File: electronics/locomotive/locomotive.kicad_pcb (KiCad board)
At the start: 2 copper layers, 16 x 64 mm, 0 parts

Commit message: electronics: locomotive: Board Rev 1.0
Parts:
- added 10: 100n, Capacitors_SMD:C_0603, F.Cu at (152.0, 92.0)
- added 10: 10k, Resistors_SMD:R_0603, F.Cu at (147.5, 112.5)
- added 11: 100n, Capacitors_SMD:C_0603, F.Cu at (144.0, 92.5)
- added 11: 10k, Resistors_SMD:R_0603, F.Cu at (156.2, 104.5)
- added 12: 10k, Resistors_SMD:R_0603, F.Cu at (144.0, 130.8)
- added 12: 1u, Capacitors_SMD:C_0603, F.Cu at (145.8, 93.5)
- added 13: 2u2, Capacitors_SMD:C_0603, F.Cu at (154.2, 125.5)
- added 13: 33k2, Resistors_SMD:R_0603, F.Cu at (151.2, 125.5)
- added 14: 26k1, Resistors_SMD:R_0603, F.Cu at (152.8, 125.5)
- added 15: 1k, Resistors_SMD:R_0603, F.Cu at (156.2, 76.2)
- added 16: 1k, Resistors_SMD:R_0603, F.Cu at (154.8, 76.2)
- added 19: 1k5, Resistors_SMD:R_0603, F.Cu at (155.5, 66.0)
- added 20: 10k, Resistors_SMD:R_0603, F.Cu at (144.5, 66.0)
- added C1: 2u2, Capacitors_SMD:C_0603, F.Cu at (147.5, 108.5)
- added C2: 2u2, Capacitors_SMD:C_0603, F.Cu at (155.5, 109.0)
- added C3: 100n, Capacitors_SMD:C_0603, F.Cu at (152.0, 90.5)
- added C4: 10p, Capacitors_SMD:C_0603, F.Cu at (148.2, 88.2)
- added C5: 10p, Capacitors_SMD:C_0603, F.Cu at (145.0, 91.5)
- added C6: 4u7, Capacitors_SMD:C_0603, F.Cu at (147.5, 111.0)
- added C7: 100n, Capacitors_SMD:C_0603, F.Cu at (143.8, 104.5)
- added C8: 100n, Capacitors_SMD:C_0603, F.Cu at (147.5, 109.8)
- added C9: 100n, Capacitors_SMD:C_0603, F.Cu at (156.2, 107.0)
- added D1: CDBHM240L-HF, bcan:TO-269AA, F.Cu at (150.0, 78.0)
- added D2: CUS08F30, Diodes_SMD:D_SOD-323, F.Cu at (145.5, 125.0)
- added D3: 1N4148, Diodes_SMD:D_SOD-523, F.Cu at (154.0, 66.0)
- added J1: PIN[1..32], bcan:Castellations_1x32_Pitch2.00mm, F.Cu at (142.0, 69.0)
- added J2: PIN[33..64], bcan:Castellations_1x32_Pitch2.00mm, F.Cu at (158.0, 131.0)
- added J3: JTAG, Pin_Headers:Pin_Header_Straight_2x05_Pitch1.27mm_SMD, B.Cu at (150.0, 90.0)
- added J4: USB_OTG, bcan:USB_Micro-B_Amphenol_10118192, F.Cu at (150.0, 130.6)
- added J5: RAILS, bcan:Castellations_1x02_Pitch2.00mm, F.Cu at (142.0, 65.0)
- added J6: MOTOR, bcan:Castellations_1x02_Pitch2.00mm, F.Cu at (158.0, 67.0)
- added J7: TRAIN, Pin_Headers:Pin_Header_Straight_2x04_Pitch2.54mm_SMD, B.Cu at (150.0, 71.5)
- added J8: IR, Connectors_JST:JST_GH_BM04B-GHS-TBT_04x1.25mm_Straight, F.Cu at (150.0, 120.0)
- added J9: TOF, Connectors_JST:JST_GH_SM04B-GHS-TB_04x1.25mm_Angled, F.Cu at (150.0, 84.0)
- added JP1: BOOT0, bcan:Solder_Jumper_NC, B.Cu at (150.0, 77.8)
- added JP2: BOOT1, bcan:Solder_Jumper_NC, B.Cu at (149.0, 123.8)
- added JP3: VCAP1, bcan:Solder_Jumper_NO, B.Cu at (149.2, 108.0)
- added JP4: VCAP2, bcan:Solder_Jumper_NO, B.Cu at (150.8, 108.0)
- added JP5: USB_VBUS, bcan:Solder_Jumper_NC, B.Cu at (151.0, 123.8)
- added L1: 600, Capacitors_SMD:C_0603, F.Cu at (143.8, 95.5)
- added Q1: MMBT2222A, TO_SOT_Packages_SMD:SOT-23, F.Cu at (155.2, 73.2)
- added Q2: MMBT2222A, TO_SOT_Packages_SMD:SOT-23, F.Cu at (144.8, 69.8)
- added Q3: DMG6601LVT, TO_SOT_Packages_SMD:SOT-23-6, F.Cu at (155.2, 69.8)
- added Q4: DMG6601LVT, TO_SOT_Packages_SMD:SOT-23-6, F.Cu at (144.8, 73.2)
- added R1: 10k, Resistors_SMD:R_0603, F.Cu at (154.8, 78.8)
- added R17: 100, Resistors_SMD:R_2512, F.Cu at (151.8, 71.5)
- added R18: 100, Resistors_SMD:R_2512, F.Cu at (148.2, 71.5)
- added R2: 10k, Resistors_SMD:R_0603, F.Cu at (149.5, 115.0)
- added R3: 10k, Resistors_SMD:R_0603, F.Cu at (152.0, 89.0)
- added R4: 13k3, Resistors_SMD:R_0603, F.Cu at (144.2, 86.2)
- added R5: 2k8, Resistors_SMD:R_0603, F.Cu at (144.2, 87.8)
- added R8: 4k7, Resistors_SMD:R_0603, F.Cu at (147.5, 115.5)
- added R9: 4k7, Resistors_SMD:R_0603, F.Cu at (147.5, 114.0)
- added U1: STM32F405RGTx, Housings_QFP:TQFP-64_10x10mm_Pitch0.5mm, F.Cu at (150.0, 100.0)
- added U2: M95512-RDW6TP, Housings_SSOP:TSSOP-8_4.4x3mm_Pitch0.65mm, F.Cu at (153.0, 112.0)
- added U5: SPX3819M5, TO_SOT_Packages_SMD:SOT-23-5, F.Cu at (148.5, 125.0)
- added U7: TLP293, Housings_SSOP:SOP-4_4.4x2.8mm_Pitch1.27mm, F.Cu at (149.2, 66.0)
- added Y1: 16MHz, Crystals:Crystal_SMD_3225-4pin_3.2x2.5mm, F.Cu at (147.0, 90.2)
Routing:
- net GND: track 0.00 -> 222.6 mm, vias 0 -> 16
- net 2V8: track 0.00 -> 124.7 mm, vias 0 -> 4
- net VCC: track 0.00 -> 93.9 mm, vias 0 -> 2
- net PA10: track 0.00 -> 51.8 mm, vias 0 -> 2
- net PA11: track 0.00 -> 48.7 mm, vias 0 -> 2
- net PA12: track 0.00 -> 47.3 mm, vias 0 -> 2
- net PB11: track 0.00 -> 47.1 mm, vias 0 -> 2
- net PB12: track 0.00 -> 46.7 mm, vias 0 -> 1
- net PB10: track 0.00 -> 45.0 mm, vias 0 -> 2
- net PB14: track 0.00 -> 43.8 mm, vias 0 -> 2
- net NRST: track 0.00 -> 42.8 mm, vias 0 -> 2
- net PC13: track 0.00 -> 39.1 mm, vias 0 -> 1
- net PA13: track 0.00 -> 37.5 mm, vias 0 -> 1
- net PB13: track 0.00 -> 35.1 mm
- net BOOT0: track 0.00 -> 33.8 mm
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- added copper zone on F.Cu, net 2V8
- added copper zone on B.Cu, net GND
- added copper zone on F.Cu, net GND
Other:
- board size 16 x 64 mm -> 16 x 68 mm
- net class Default: clearance 0.2 -> 0.16; trace_width 0.25 -> 0.2
- net class Motor added: clearance 0.16, trace_width 0.6, via_dia 0.6, via_drill 0.4
- net class Power added: clearance 0.16, trace_width 0.3, via_dia 0.6, via_drill 0.4
- rule trace_clearance: 0.2 -> 0.16
- board text added: "+"
- board text added: "-"
- board text added: "2V8"
- board text added: "5V"
- board text added: "B8"
- board text added: "B9"
- board text added: "BOOT0"
- board text added: "BOOT1"
- board text added: "C13"
- board text added: "C14"
- board text added: "C15"
- board text added: "F-"
- board text added: "GND"
- board text added: "IR"
- board text added: "JST-GH"
- board text added: "JTAG"
- board text added: "L"
- board text added: "Locomotive Rev 1.0"
- board text added: "MOTOR"
- board text added: "NRST"
- board text added: "PA0"
- board text added: "PA1"
- board text added: "PA10"
- board text added: "PA11"
- board text added: "PA12"
- board text added: "PA13"
- board text added: "PA14"
- board text added: "PA15"
- board text added: "PA2"
- board text added: "PA3"
- board text added: "PA4"
- board text added: "PA5"
- board text added: "PA6"
- board text added: "PA7"
- board text added: "PA8"
- board text added: "PA9"
- board text added: "PB0"
- board text added: "PB1"
- board text added: "PB10"
- board text added: "PB11"
- board text added: "PB12"
- board text added: "PB13"
- board text added: "PB14"
- board text added: "PB15"
- board text added: "PB2"
- board text added: "PB3"
- board text added: "PB4"
- board text added: "PB5"
- board text added: "PB6"
- board text added: "PB7"
- board text added: "PC0"
- board text added: "PC1"
- board text added: "PC10"
- board text added: "PC11"
- board text added: "PC12"
- board text added: "PC2"
- board text added: "PC3"
- board text added: "PC4"
- board text added: "PC5"
- board text added: "PC6"
- board text added: "PC7"
- board text added: "PC8"
- board text added: "PC9"
- board text added: "PD2"
- board text added: "R"
- board text added: "R-"
- board text added: "RAILS"
- board text added: "TOF"
- board text added: "VBAT"
- board text added: "VCAP"
- board text added: "VCC"
- board text added: "bcan.io"

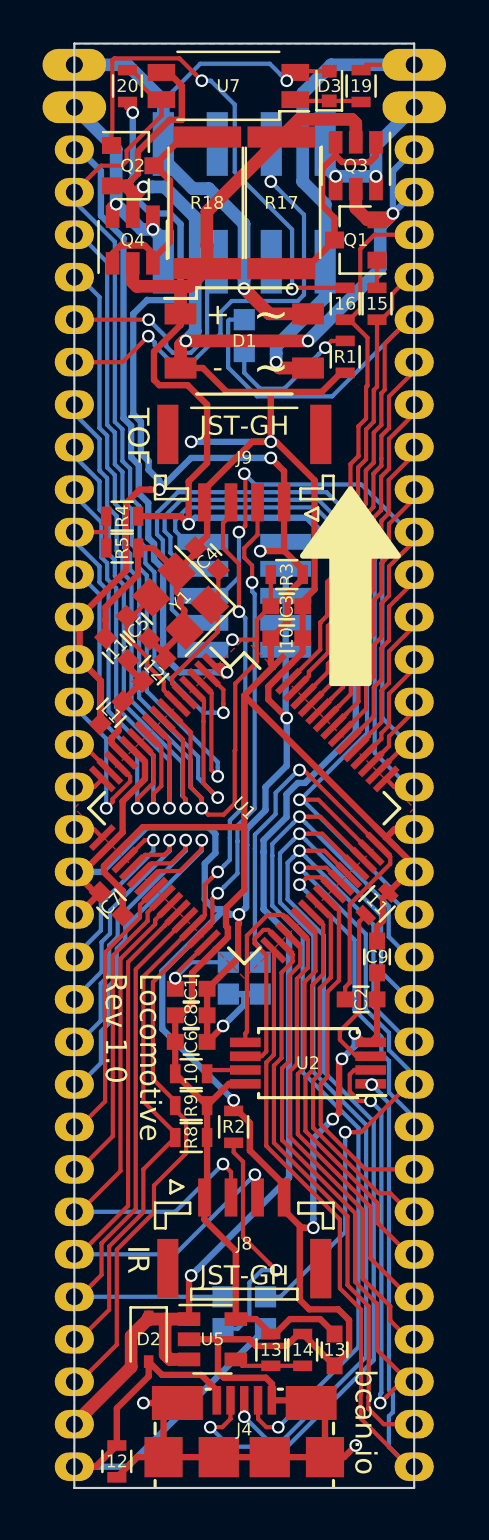
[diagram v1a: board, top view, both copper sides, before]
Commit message: electronics: locomotive: Fix mislabeled parts
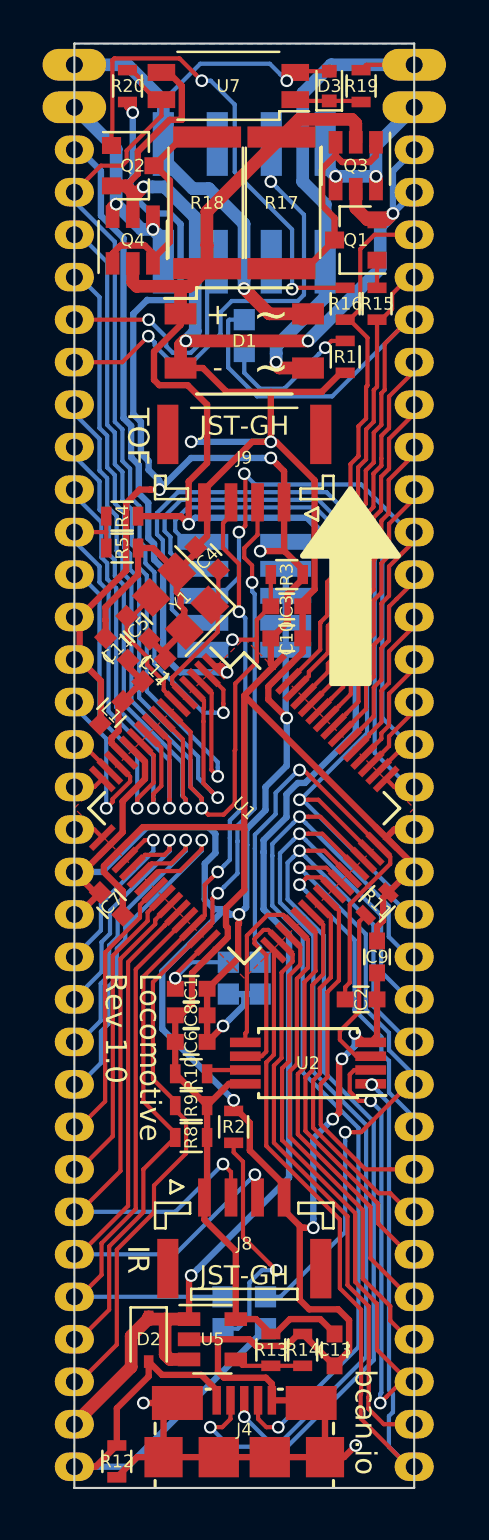
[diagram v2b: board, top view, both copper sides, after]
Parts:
- renumbered 10 to C10, 11 to C11, 12 to C12, 13 to C13, 10 to R10, 11 to R11, 12 to R12, 13 to R13, 14 to R14, 15 to R15, 16 to R16, 19 to R19, 20 to R20
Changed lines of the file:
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@@
     (tags "resistor 0603")
     (attr smd)
-    (fp_text reference 20 (at 0 0 180) (layer F.SilkS)
+    (fp_text reference R20 (at 0 0 180) (layer F.SilkS)
       (effects (font (size 0.6 0.6) (thickness 0.1)))
     )
@@
     (tags "resistor 0603")
     (attr smd)
-    (fp_text reference 16 (at 0 0 360) (layer F.SilkS)
+    (fp_text reference R16 (at 0 0 360) (layer F.SilkS)
       (effects (font (size 0.6 0.6) (thickness 0.1)))
     )
@@
     (tags "resistor 0603")
     (attr smd)
-    (fp_text reference 12 (at 0 0 360) (layer F.SilkS)
+    (fp_text reference R12 (at 0 0 360) (layer F.SilkS)
       (effects (font (size 0.6 0.6) (thickness 0.1)))
     )
@@
     (tags "resistor 0603")
     (attr smd)
-    (fp_text reference 15 (at 0 0 360) (layer F.SilkS)
+    (fp_text reference R15 (at 0 0 360) (layer F.SilkS)
       (effects (font (size 0.6 0.6) (thickness 0.1)))
     )
@@
     (tags "capacitor 0603")
     (attr smd)
-    (fp_text reference 10 (at 0 0 90) (layer F.SilkS)
+    (fp_text reference C10 (at 0 0 90) (layer F.SilkS)
       (effects (font (size 0.6 0.6) (thickness 0.1)))
     )
@@
     (tags "capacitor 0603")
     (attr smd)
-    (fp_text reference 11 (at 0 0 225) (layer F.SilkS)
+    (fp_text reference C11 (at 0 0 225) (layer F.SilkS)
       (effects (font (size 0.6 0.6) (thickness 0.1)))
     )
@@
     (tags "capacitor 0603")
     (attr smd)
-    (fp_text reference 12 (at 0 0 135) (layer F.SilkS)
+    (fp_text reference C12 (at 0 0 135) (layer F.SilkS)
       (effects (font (size 0.6 0.6) (thickness 0.1)))
     )
@@
     (tags "capacitor 0603")
     (attr smd)
-    (fp_text reference 13 (at 0 0 360) (layer F.SilkS)
+    (fp_text reference C13 (at 0 0 360) (layer F.SilkS)
       (effects (font (size 0.6 0.6) (thickness 0.1)))
     )
@@
     (tags "resistor 0603")
     (attr smd)
-    (fp_text reference 10 (at 0 0 90) (layer F.SilkS)
+    (fp_text reference R10 (at 0 0 90) (layer F.SilkS)
       (effects (font (size 0.6 0.6) (thickness 0.1)))
     )
@@
     (tags "resistor 0603")
     (attr smd)
-    (fp_text reference 11 (at 0 0 315) (layer F.SilkS)
+    (fp_text reference R11 (at 0 0 315) (layer F.SilkS)
       (effects (font (size 0.6 0.6) (thickness 0.1)))
     )
@@
     (tags "resistor 0603")
     (attr smd)
-    (fp_text reference 13 (at 0 0 360) (layer F.SilkS)
+    (fp_text reference R13 (at 0 0 360) (layer F.SilkS)
       (effects (font (size 0.6 0.6) (thickness 0.1)))
     )
@@
     (tags "resistor 0603")
     (attr smd)
-    (fp_text reference 14 (at 0 0 180) (layer F.SilkS)
+    (fp_text reference R14 (at 0 0 180) (layer F.SilkS)
       (effects (font (size 0.6 0.6) (thickness 0.1)))
     )
@@
     (tags "resistor 0603")
     (attr smd)
-    (fp_text reference 19 (at 0 0 180) (layer F.SilkS)
-      (effects (font (size 0.6 0.6) (thickness 0.1)))
-    )
+    (fp_text reference R19 (at 0 0 180) (layer F.SilkS)
+      (effects (font (size 0.6 0.6) (thickness 0.1)))
+    )
